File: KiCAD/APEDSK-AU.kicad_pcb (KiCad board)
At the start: 4 copper layers, 71.1 x 68.6 mm, 25 parts, among them J1 240-44-44Pins, P1 Power, P2 Analog, P3 Digital, P4 Digital, U1 74LS245, U2 74LS541, U3 74LS541, U4 74LS138, U5 74HC595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

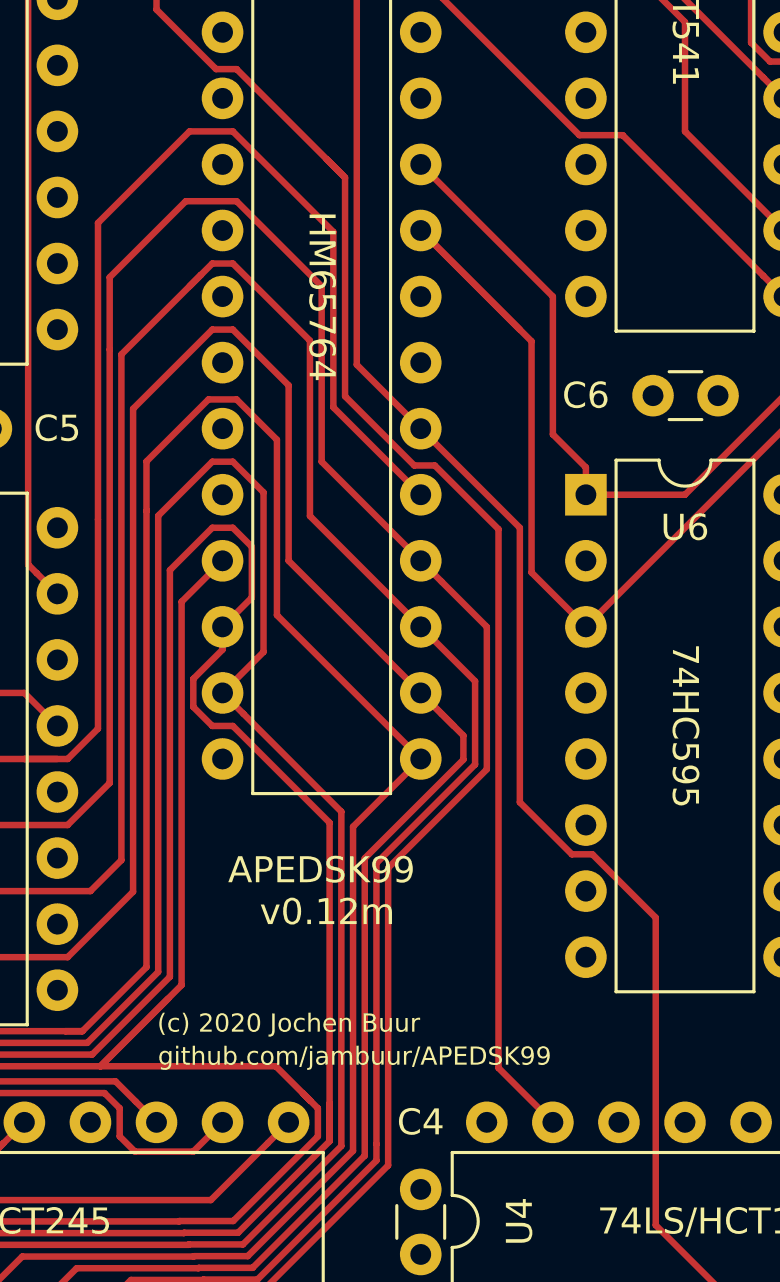
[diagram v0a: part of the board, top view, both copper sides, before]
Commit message: Added R5 for D2:TI_INT/ETH_CS shared use
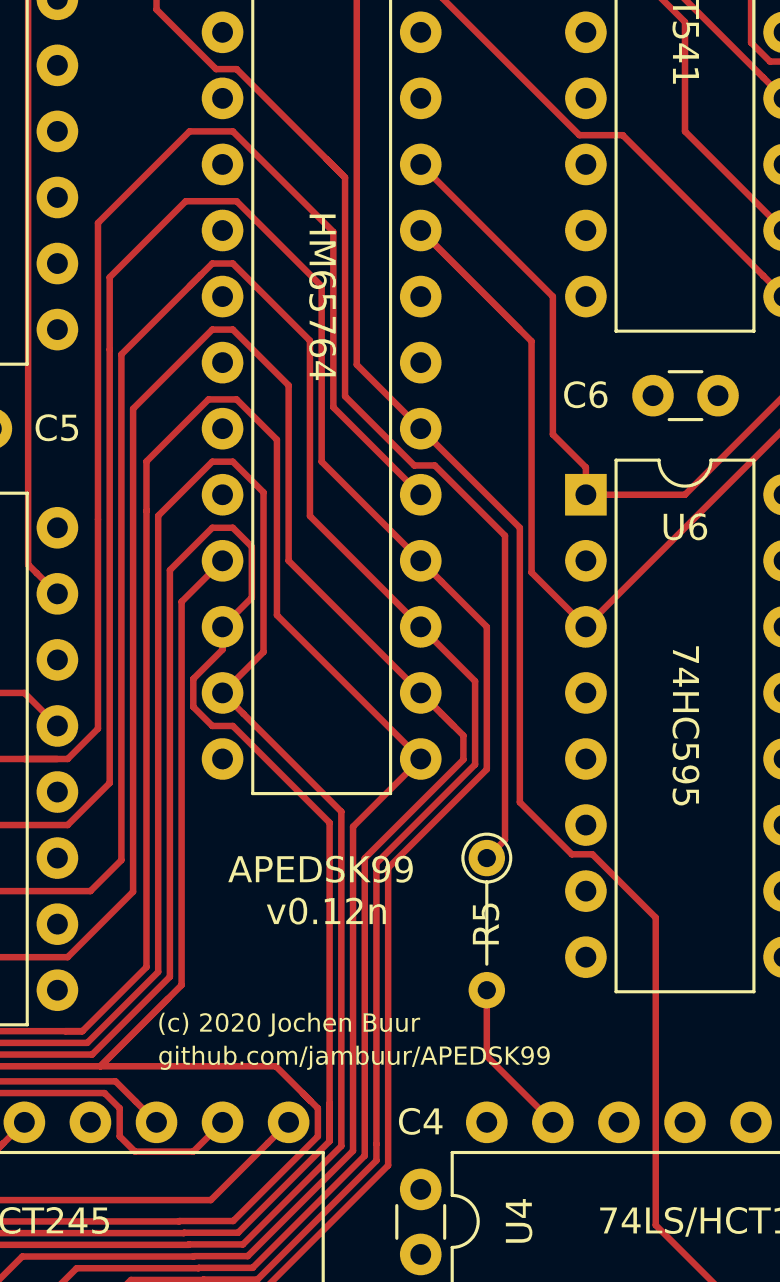
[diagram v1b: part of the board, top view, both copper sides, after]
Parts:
- added R5: 1K, Resistor_THT:R_Axial_DIN0204_L3.6mm_D1.6mm_P5.08mm_Vertical, F.Cu at (152.9, 116.2)
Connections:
- U4 pad 15: /~TI_INT -> Net-(R5-Pad2)
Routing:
- net /~TI_INT: track 73.2 -> 62.6 mm
- net Net-(R5-Pad2): track 0.00 -> 6.13 mm
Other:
- board text added: "APEDSK99 v0.12n"
- board text removed: "APEDSK99 v0.12m"
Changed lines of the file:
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@@
     (thickness 1.6)
     (drawings 86)
-    (tracks 913)
+    (tracks 915)
     (zones 0)
-    (modules 25)
-    (nets 100)
+    (modules 26)
+    (nets 101)
   )
   (page A4)
@@
   )
   (layers
-    (0 Top-Data signal hide)
-    (1 Layer2-Power mixed)
+    (0 Top-Data signal)
+    (1 Layer2-Power mixed hide)
     (2 Layer3-Address signal hide)
     (31 Bottom-GND power hide)
-    (36 B.SilkS user)
-    (37 F.SilkS user hide)
+    (36 B.SilkS user hide)
+    (37 F.SilkS user)
     (38 B.Mask user hide)
     (39 F.Mask user)
@@
   (net 98 /CE_245)
   (net 99 /~TI_INT)
+  (net 100 "Net-(R5-Pad2)")
   (net_class Default "This is the default net class."
     (clearance 0.2)
@@
     (add_net "Net-(P3-Pad7)")
     (add_net "Net-(P3-Pad8)")
+    (add_net "Net-(R5-Pad2)")
     (add_net "Net-(U4-Pad10)")
     (add_net "Net-(U4-Pad11)")
@@
     (add_net "Net-(U6-Pad9)")
     (add_net "Net-(U7-Pad1)")
+  )
+  (module Resistor_THT:R_Axial_DIN0204_L3.6mm_D1.6mm_P5.08mm_Vertical (layer Top-Data)
+    (at 152.908 116.205 270)
+    (descr "Resistor, Axial_DIN0204 series, Axial, Vertical, pin pitch=5.08mm, 0.167W, length*diameter=3.6*1.6mm^2, http://cdn-reichelt.de/documents/datenblatt/B400/1_4W%23YAG.pdf")
+    (tags "Resistor Axial_DIN0204 series Axial Vertical pin pitch 5.08mm 0.167W length 3.6mm diameter 1.6mm")
+    (fp_text reference R5 (at 2.54 0 90) (layer F.SilkS)
+      (effects (font (size 1 1) (thickness 0.15)))
+    )
+    (fp_text value 1K (at 2.54 1.92 90) (layer F.Fab)
+      (effects (font (size 1 1) (thickness 0.15)))
+    )
+    (fp_text user %R (at 2.54 -1.92 90) (layer F.Fab)
+      (effects (font (size 1 1) (thickness 0.15)))
+    )
+    (fp_line (start 6.03 -1.05) (end -1.05 -1.05) (layer F.CrtYd) (width 0.05))
+    (fp_line (start 6.03 1.05) (end 6.03 -1.05) (layer F.CrtYd) (width 0.05))
+    (fp_line (start -1.05 1.05) (end 6.03 1.05) (layer F.CrtYd) (width 0.05))
+    (fp_line (start -1.05 -1.05) (end -1.05 1.05) (layer F.CrtYd) (width 0.05))
+    (fp_line (start 0.92 0) (end 4.08 0) (layer F.SilkS) (width 0.12))
+    (fp_line (start 0 0) (end 5.08 0) (layer F.Fab) (width 0.1))
+    (fp_circle (center 0 0) (end 0.92 0) (layer F.SilkS) (width 0.12))
+    (fp_circle (center 0 0) (end 0.8 0) (layer F.Fab) (width 0.1))
+    (pad 2 thru_hole oval (at 5.08 0 270) (size 1.4 1.4) (drill 0.7) (layers *.Cu *.Mask)
+      (net 100 "Net-(R5-Pad2)"))
+    (pad 1 thru_hole circle (at 0 0 270) (size 1.4 1.4) (drill 0.7) (layers *.Cu *.Mask)
+      (net 99 /~TI_INT))
+    (model ${KISYS3DMOD}/Resistor_THT.3dshapes/R_Axial_DIN0204_L3.6mm_D1.6mm_P5.08mm_Vertical.wrl
+      (at (xyz 0 0 0))
+      (scale (xyz 1 1 1))
+      (rotate (xyz 0 0 0))
+    )
   )
   (module Resistor_THT:R_Axial_DIN0204_L3.6mm_D1.6mm_P5.08mm_Vertical (layer Top-Data)
@@
       (net 2 GND))
     (pad 15 thru_hole oval (at 7.62 2.54 90) (size 1.6 1.6) (drill 0.8) (layers *.Cu *.Mask)
-      (net 99 /~TI_INT))
+      (net 100 "Net-(R5-Pad2)"))
     (pad 7 thru_hole oval (at 0 15.24 90) (size 1.6 1.6) (drill 0.8) (layers *.Cu *.Mask)
       (net 78 "Net-(U4-Pad7)"))
@@
     (effects (font (size 0.7 0.7) (thickness 0.15)))
   )
-  (gr_text "APEDSK99\n v0.12m" (at 146.558 117.475) (layer F.SilkS)
+  (gr_text "APEDSK99\n v0.12n" (at 146.558 117.475) (layer F.SilkS)
     (effects (font (size 1 1) (thickness 0.15)))
   )
@@
   (segment (start 142.497997 85.869999) (end 143.288001 85.869999) (width 0.25) (layer Top-Data) (net 99))
   (segment (start 123.698 78.105) (end 124.964 78.105) (width 0.25) (layer Top-Data) (net 99) (status 10))
-  (segment (start 147.458022 90.04002) (end 146.755501 89.337499) (width 0.25) (layer Top-Data) (net 99))
-  (segment (start 147.458022 98.450024) (end 147.458022 90.04002) (width 0.25) (layer Top-Data) (net 99))
-  (segment (start 150.117997 101.109999) (end 147.458022 98.450024) (width 0.25) (layer Top-Data) (net 99))
   (segment (start 143.288001 85.869999) (end 146.755501 89.337499) (width 0.25) (layer Top-Data) (net 99))
-  (segment (start 155.448 126.365) (end 153.358008 124.275008) (width 0.25) (layer Top-Data) (net 99) (status 10))
-  (segment (start 153.358008 124.275008) (end 153.358008 103.560006) (width 0.25) (layer Top-Data) (net 99))
   (segment (start 146.755501 89.337499) (end 147.377989 89.959987) (width 0.25) (layer Top-Data) (net 99))
-  (segment (start 153.358008 103.560006) (end 150.908001 101.109999) (width 0.25) (layer Top-Data) (net 99))
-  (segment (start 150.908001 101.109999) (end 150.117997 101.109999) (width 0.25) (layer Top-Data) (net 99))
+  (segment (start 153.607999 115.505001) (end 152.908 116.205) (width 0.25) (layer Top-Data) (net 99))
+  (segment (start 146.755501 89.337499) (end 147.458022 90.04002) (width 0.25) (layer Top-Data) (net 99))
+  (segment (start 147.458022 90.04002) (end 147.458022 98.450024) (width 0.25) (layer Top-Data) (net 99))
+  (segment (start 150.117997 101.109999) (end 150.908001 101.109999) (width 0.25) (layer Top-Data) (net 99))
+  (segment (start 147.458022 98.450024) (end 150.117997 101.109999) (width 0.25) (layer Top-Data) (net 99))
+  (segment (start 150.908001 101.109999) (end 153.607999 103.809997) (width 0.25) (layer Top-Data) (net 99))
+  (segment (start 153.607999 103.809997) (end 153.607999 115.505001) (width 0.25) (layer Top-Data) (net 99))
+  (segment (start 152.908 123.825) (end 155.448 126.365) (width 0.25) (layer Top-Data) (net 100))
+  (segment (start 152.908 121.285) (end 152.908 123.825) (width 0.25) (layer Top-Data) (net 100))
   (zone (net 2) (net_name GND) (layer Bottom-GND) (hatch edge 0.508)
     (connect_pads (clearance 0.508))

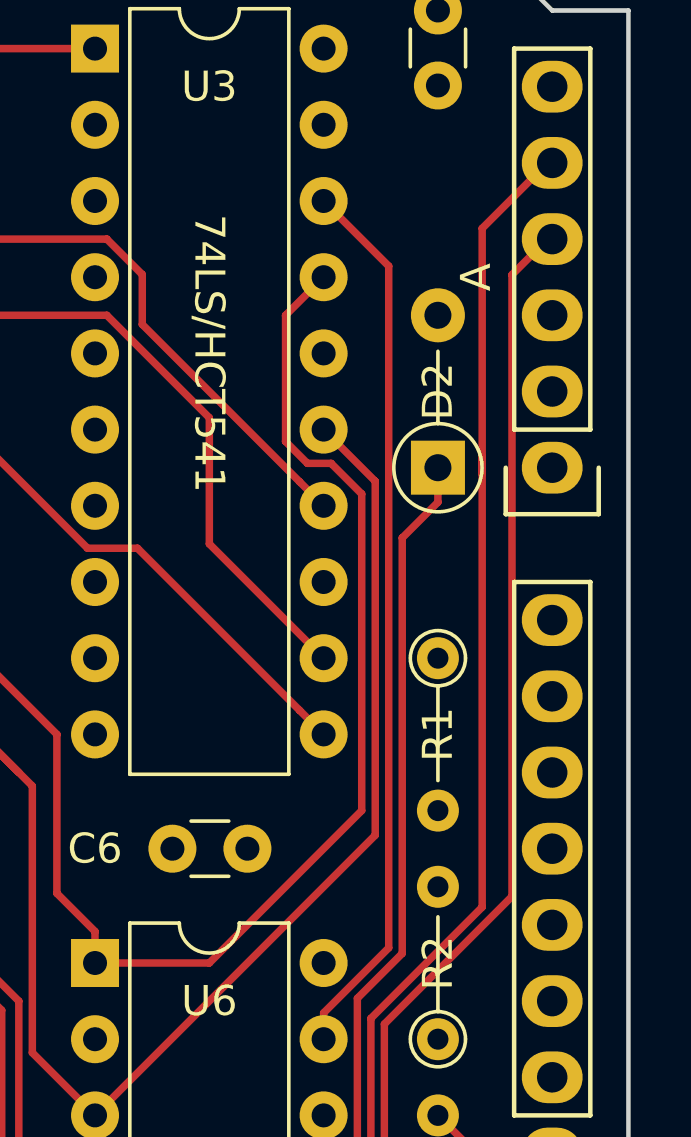
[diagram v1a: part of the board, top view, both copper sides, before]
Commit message: added R6 noise supression resistor
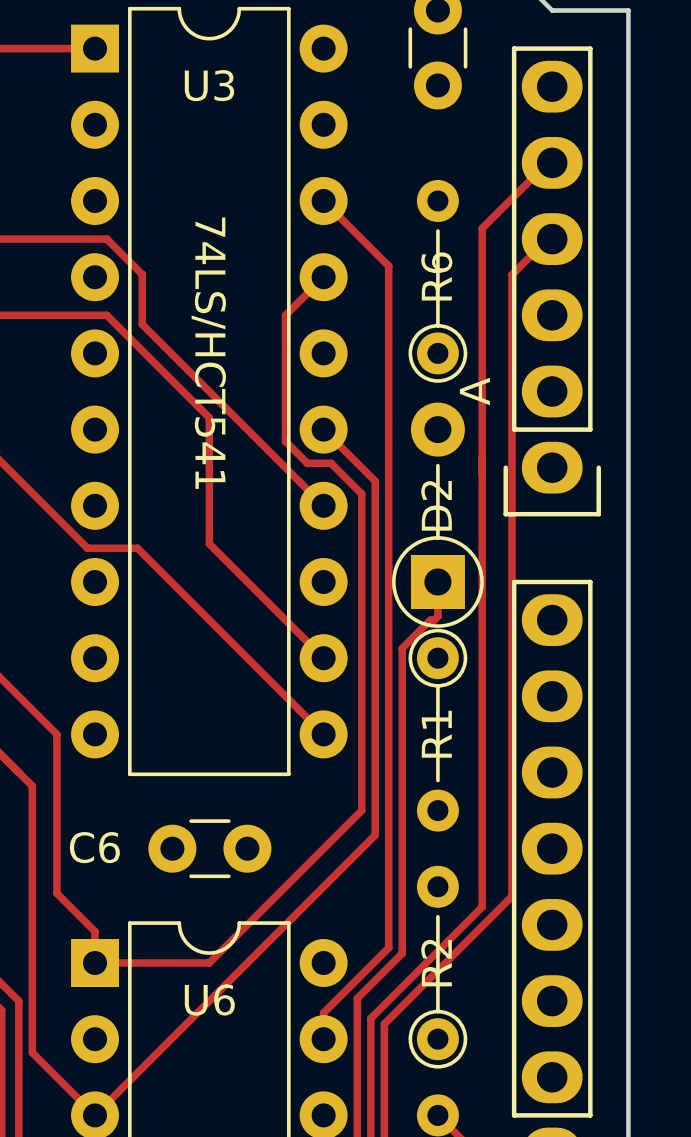
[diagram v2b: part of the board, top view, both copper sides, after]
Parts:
- added R6: 1K, Resistor_THT:R_Axial_DIN0204_L3.6mm_D1.6mm_P5.08mm_Vertical, F.Cu at (168.1, 81.9)
- D2: value 1N5711 -> 1N4148
- moved D2 3.81 mm to (168.1, 89.5)
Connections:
- D2 pad 2: /READY -> Net-(D2-Pad2)
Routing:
- net /~AD_WE: track 91.5 -> 99.9 mm
- net /READY: track 110.1 -> 113.9 mm
- net /~AR_BUF: track 94.0 -> 90.2 mm
- net Net-(D2-Pad2): track 0.00 -> 2.54 mm
- net /~TIBUF: track 81.8 -> 84.0 mm
- net /DS: track 58.9 -> 59.5 mm

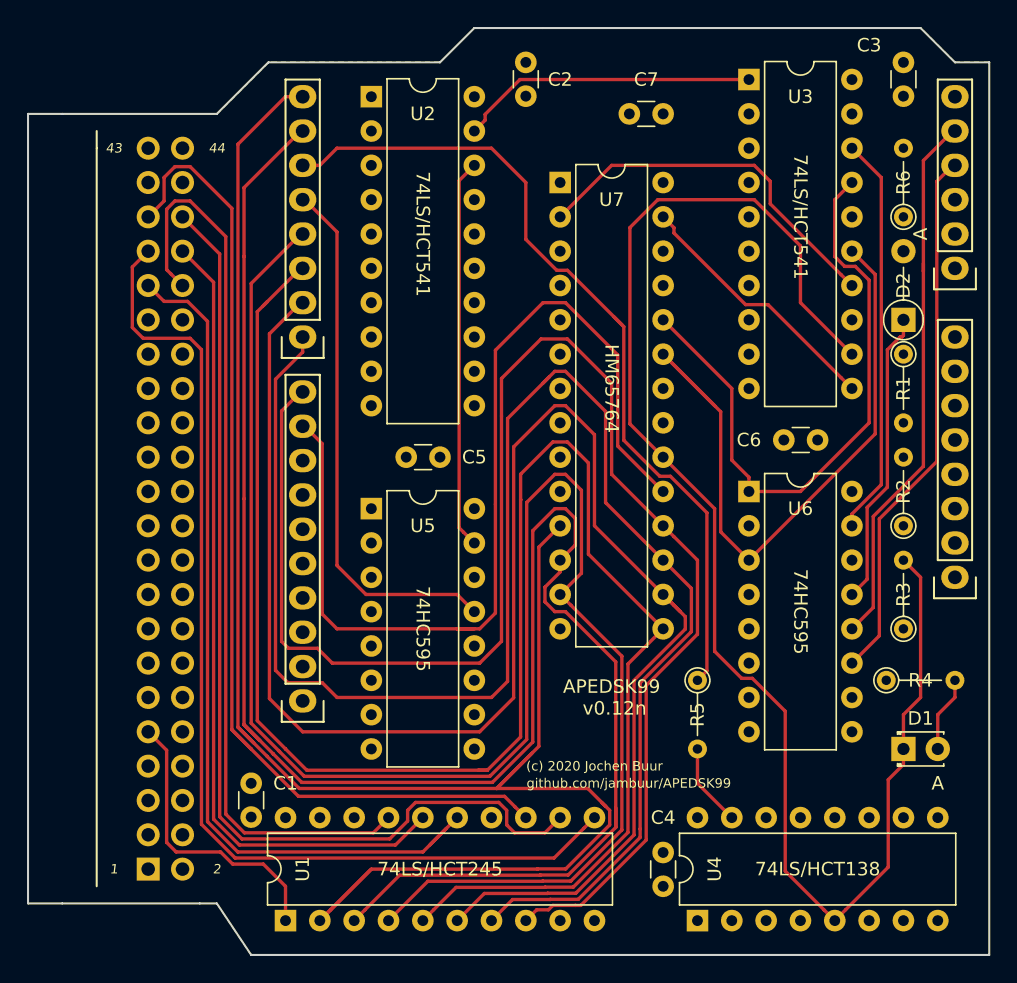
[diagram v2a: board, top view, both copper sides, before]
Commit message: APEETH99 -> APEDSK99
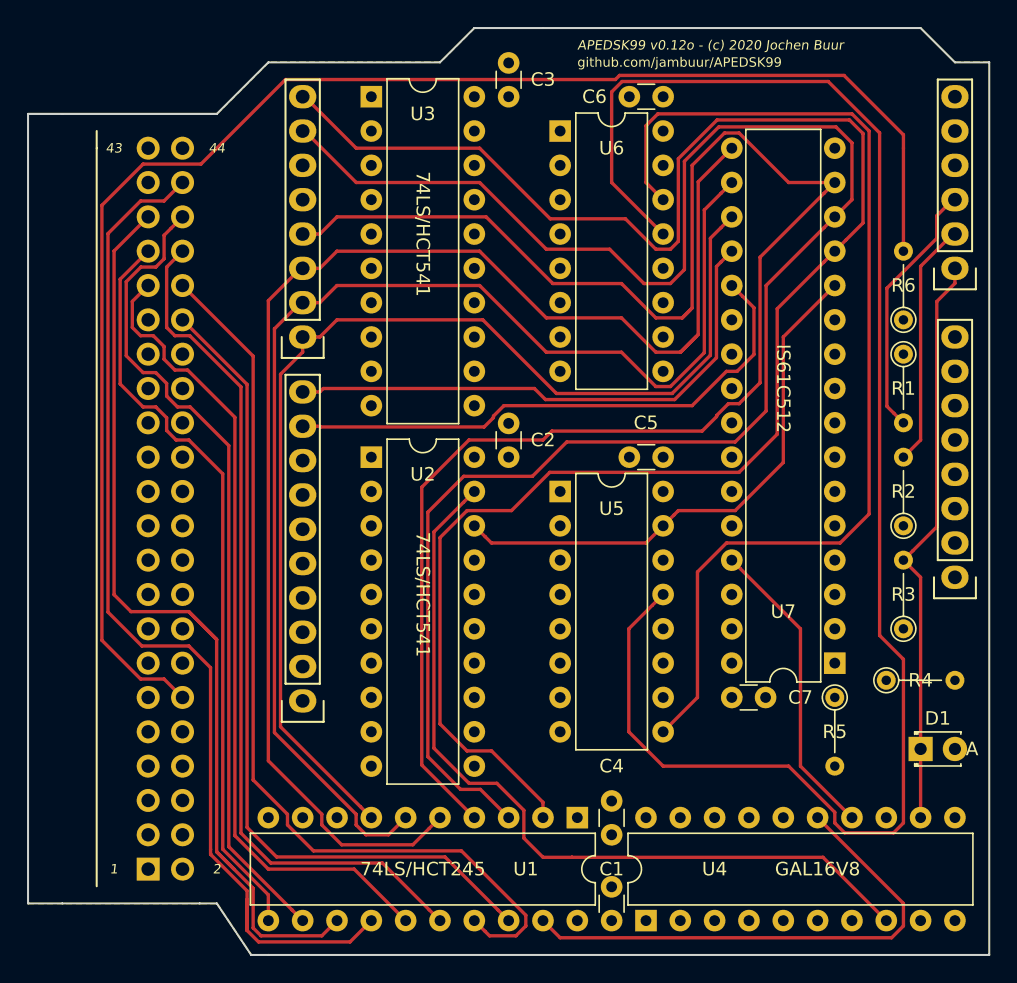
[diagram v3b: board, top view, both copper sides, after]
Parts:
- removed D2: 1N4148, Diode_THT:D_A-405_P5.08mm_Vertical_AnodeUp
- U4: value 74LS138 -> GAL16V8; footprint Package_DIP:DIP-16_W7.62mm -> Package_DIP:DIP-20_W7.62mm
- U7: value HM65764 -> IS61C512-20M; footprint Package_DIP:DIP-28_W7.62mm -> Package_DIP:DIP-32_W7.62mm
- moved C7 43.5 mm to (155.4, 117.5), turned to 0 degrees
- moved U7 41.0 mm to (163.1, 114.9), turned to 180 degrees
- moved U6 30.1 mm to (142.7, 75.6)
- moved C3 29.2 mm to (138.9, 73.0)
- moved U3 28.0 mm to (128.8, 73.0)
- moved C1 27.7 mm to (146.6, 134.0)
- moved C6 26.9 mm to (150.4, 73.0), turned to 180 degrees
- moved C2 26.7 mm to (138.9, 99.7)
- moved U2 26.7 mm to (128.8, 99.7)
- moved U1 22.9 mm to (144.0, 126.4), turned to 270 degrees
- moved C5 16.5 mm to (150.4, 99.7)
- moved U5 14.0 mm to (142.7, 102.2)
- moved R5 10.2 mm to (163.1, 117.5)
- moved R6 7.62 mm to (168.1, 89.5)
- moved C4 5.39 mm to (146.6, 127.6)
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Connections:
- J1 pad 20: Net-(J1-Pad20) -> /A2
- J1 pad 28: /~MBE -> Net-(J1-Pad28)
- J1 pad 30: Net-(J1-Pad30) -> /A1
- J1 pad 31: Net-(J1-Pad31) -> /A0
- J1 pad 32: Net-(J1-Pad32) -> /~MEMEN
- R6 pad 1: Net-(D2-Pad2) -> /~AR_BUF
- U3 pad 11: /~AD_WE -> /AD_A15
- U3 pad 12: /~AD_CE -> /AD_A14
- U3 pad 13: /CE_245 -> /AD_A13
- U3 pad 7: /~MBE -> /A2
- U3 pad 8: /~MBE -> /A1
- U3 pad 9: /~WE -> /A0
- U4 pad 10: Net-(U4-Pad10) -> GND
- U4 pad 11: Net-(U4-Pad11) -> GND
- U4 pad 12: Net-(U4-Pad12) -> /~AD_CE
- U4 pad 13: Net-(U4-Pad13) -> Net-(R5-Pad2)
- U4 pad 14: Net-(U4-Pad14) -> /~AD_WE
- U4 pad 15: Net-(R5-Pad2) -> /CE_245
- U4 pad 16: +5V -> Net-(U4-Pad16)
- U4 pad 2: GND -> /AD_A13
- U4 pad 3: GND -> /AD_A14
- U4 pad 4: /~AD_WE -> /AD_A15
- U4 pad 5: /~AD_CE -> /AD_A0
- U4 pad 6: /A15 -> /~WE
- U4 pad 7: Net-(U4-Pad7) -> /~MEMEN
- U4 pad 8: GND -> /~TIBUF
- U4 pad 9: Net-(U4-Pad9) -> GND
- U6 pad 5: Net-(U6-Pad5) -> /AD_A13
- U6 pad 6: Net-(U6-Pad6) -> /AD_A14
- U6 pad 7: Net-(U6-Pad7) -> /AD_A15
- U7 pad 10: /AD_A0 -> /AD_A2
- U7 pad 11: /AD_D0 -> /AD_A1
- U7 pad 12: /AD_D1 -> /AD_A0
- U7 pad 13: /AD_D2 -> /AD_D0
- U7 pad 14: GND -> /AD_D1
- U7 pad 15: /AD_D3 -> /AD_D2
- U7 pad 16: /AD_D4 -> GND
- U7 pad 17: /AD_D5 -> /AD_D3
- U7 pad 18: /AD_D6 -> /AD_D4
- U7 pad 19: /AD_D7 -> /AD_D5
- U7 pad 2: /AD_A12 -> Net-(U7-Pad2)
- U7 pad 20: /~AD_CE -> /AD_D6
- U7 pad 21: /AD_A10 -> /AD_D7
- U7 pad 22: GND -> /~AD_CE
- U7 pad 23: /AD_A11 -> /AD_A10
- U7 pad 24: /AD_A9 -> GND
- U7 pad 25: /AD_A8 -> /AD_A11
- U7 pad 26: +5V -> /AD_A9
- U7 pad 27: /~AD_WE -> /AD_A8
- U7 pad 28: +5V -> /AD_A13
- U7 pad 3: /AD_A7 -> /AD_A14
- U7 pad 4: /AD_A6 -> /AD_A12
- U7 pad 5: /AD_A5 -> /AD_A7
- U7 pad 6: /AD_A4 -> /AD_A6
- U7 pad 7: /AD_A3 -> /AD_A5
- U7 pad 8: /AD_A2 -> /AD_A4
- U7 pad 9: /AD_A1 -> /AD_A3
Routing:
- net /A15: track 125.6 -> 19.4 mm
- net /~AR_BUF: track 90.2 -> 193.7 mm
- net /AD_A14: track 0.00 -> 102.1 mm
- net /AD_A15: track 0.00 -> 95.9 mm
- net /AD_A13: track 0.00 -> 91.8 mm
- net /~MEMEN: track 0.00 -> 90.6 mm
- net /~AD_CE: track 139.4 -> 60.8 mm
- net /~TIBUF: track 84.0 -> 159.9 mm
- net +5V: track 239.3 -> 165.6 mm
- net /~MBE: track 71.1 -> 0.00 mm
- net /AD_D7: track 141.9 -> 72.6 mm
- net /AD_A0: track 49.2 -> 93.5 mm
- net /AD_D6: track 116.5 -> 73.3 mm
- net /A9: track 71.3 -> 29.4 mm
- net /CE_245: track 78.6 -> 38.2 mm
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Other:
- board text added: "A0"
- board text added: "A1"
- board text added: "A2"
- board text added: "APEDSK99 v0.12o - (c) 2020 Jochen Buur"
- board text added: "GAL16V8"
- board text added: "IS61C512"
- board text added: "~MEMEN"
- board text removed: "(c) 2020 Jochen Buur"
- board text removed: "74HC595"
- board text removed: "74LS/HCT138"
- board text removed: "APEDSK99 v0.12n"
- board text removed: "HM65764"
- board text removed: "~MBE"
